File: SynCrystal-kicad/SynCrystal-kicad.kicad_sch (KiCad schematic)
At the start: 93 parts, among them CN1 PJ-342, J1 ICSP, J4 Pause Button, J5 to DIN-6 Male, J6 DIN-6 male, Q1 SS8050, Q2 SS8050, Q3 AO3400A, Q4 SS8050, SW1 Mode -, SW2 Mode +, SW3 Frame -, SW4 Frame +, SW6 Guide/Follow, U1 74HCT14, U10 MCP4725, U2 ATmega328P-A, U3 AP2210N-3.3TRG1, U4 ECS-TXO-3225MV-160-TR, U5 LMC6482, U7 G3VM-61VY3(TR)

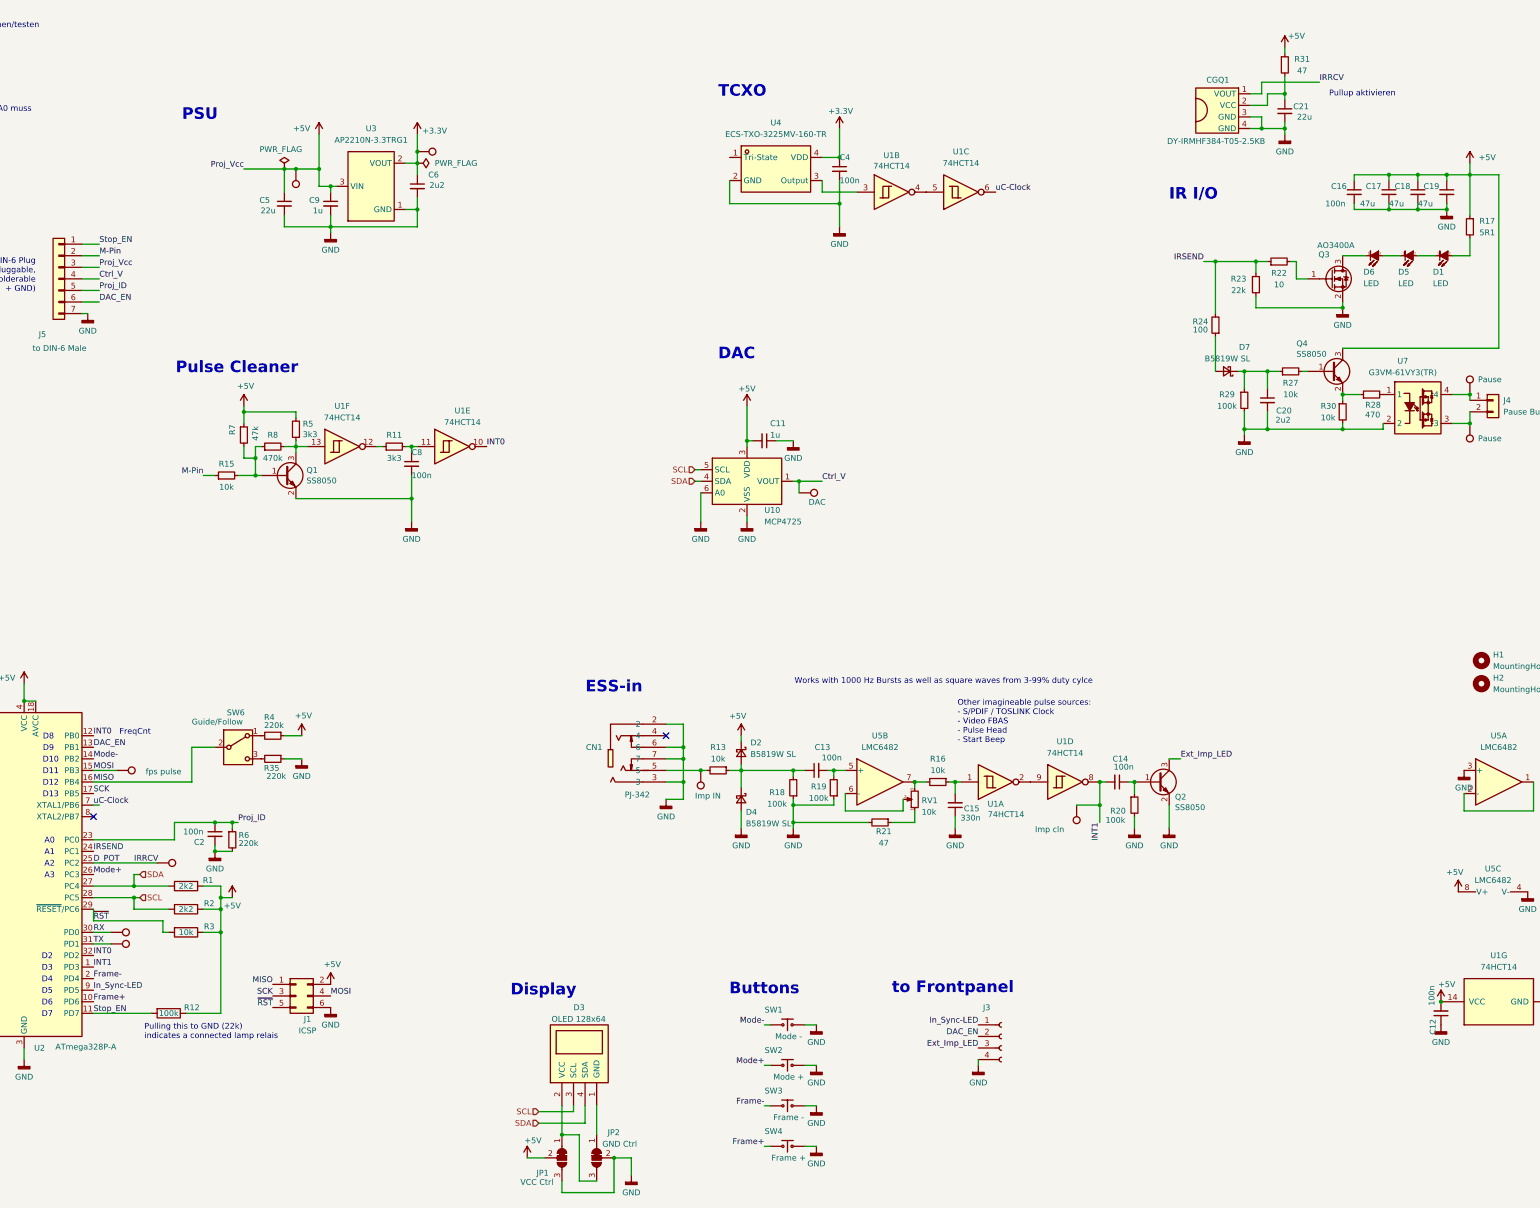
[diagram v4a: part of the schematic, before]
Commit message: ERC now happy!
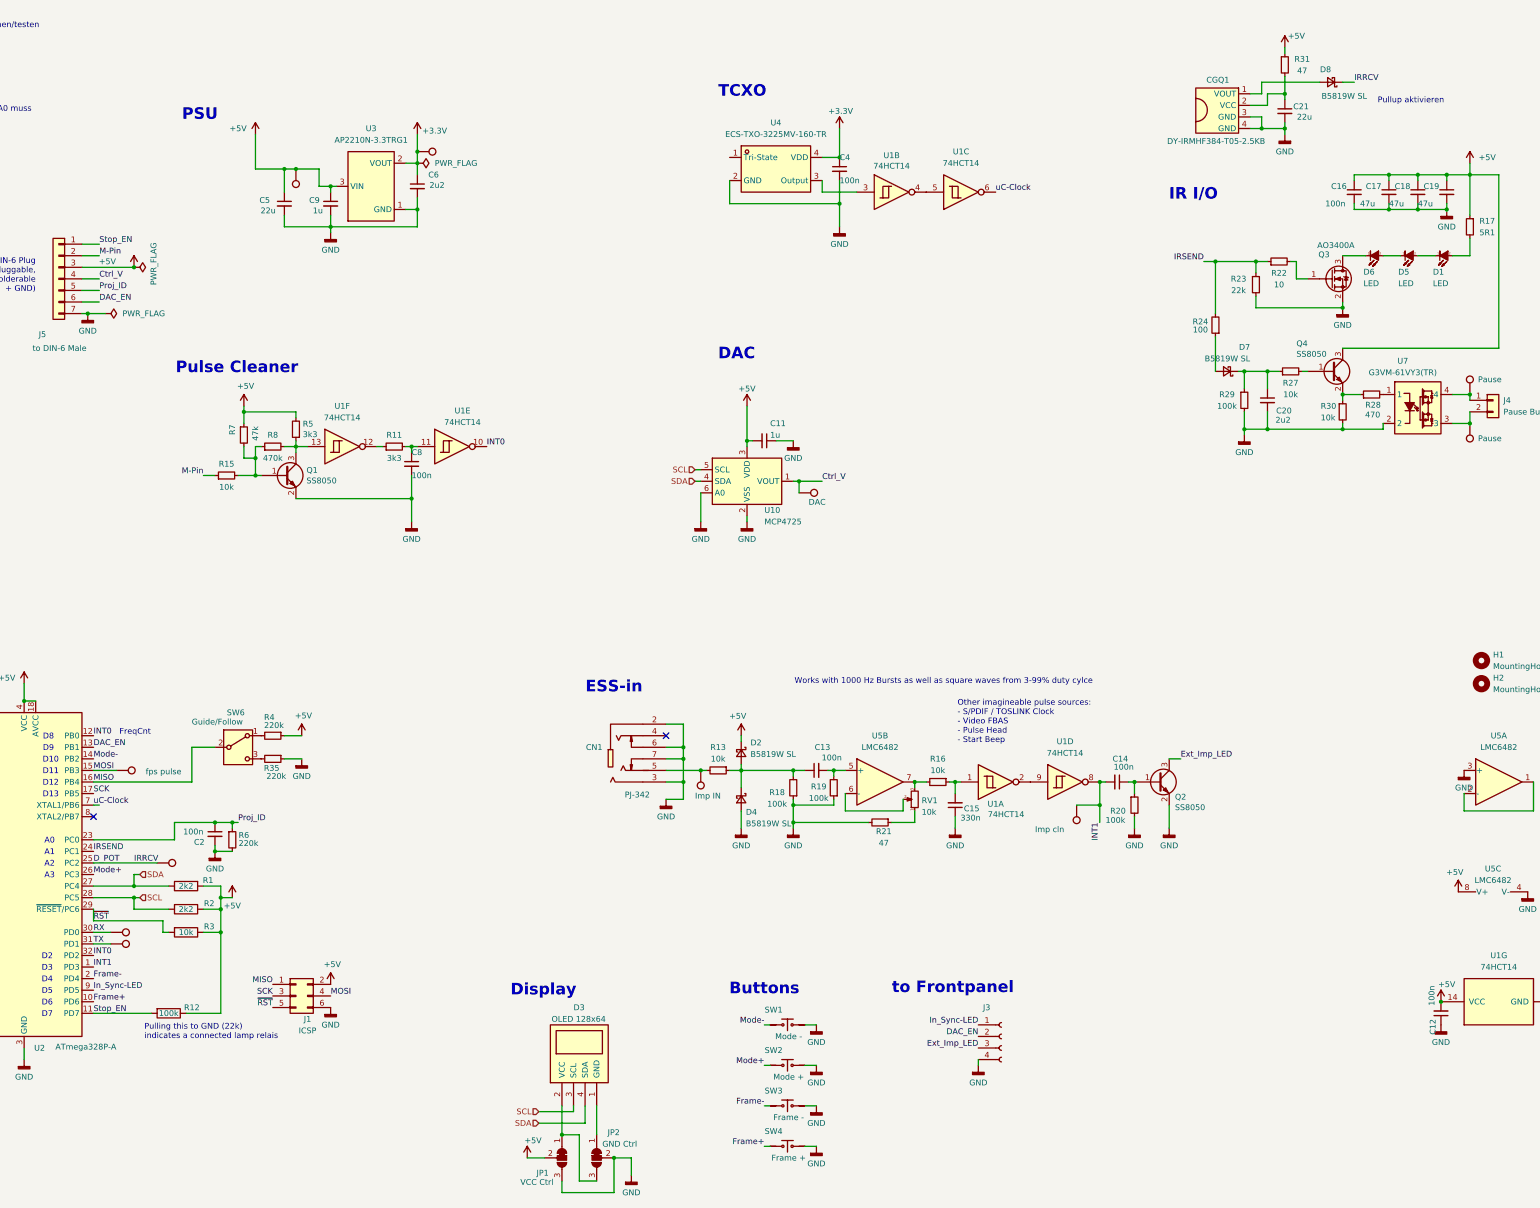
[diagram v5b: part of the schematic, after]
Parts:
- added D8: B5819W SL, Diode_SMD:D_SOD-123, symbol Device:D_Schottky_Small
- CGQ1: LCSC Part (none) -> C7280961
- CN1: LCSC Part (none) -> C668606
- D1, D5, D6: footprint easyEDA:LED-SMD_XYC-IRA4335A65-X4 -> easyeda2kicad:LED-SMD_XYC-IRA4335A65-X4
- SW1, SW2, SW3, SW4: footprint easyEDA:SW-SMD_4P-L6.0-W6.0-P4.50-LS9.0_TS-1002S-08026C -> easyEDA:KEY-SMD_4P-L6.0-W6.0-P4.50-LS8.6
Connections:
- net D_POT: now also D8.1 (K); no longer CGQ1.1 (VOUT)
- new net: CGQ1.1 (VOUT), D8.2 (A)

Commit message: Reannotated, PCB now messed up :)
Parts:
- D2: renamed from D6; footprint easyeda2kicad:LED-SMD_XYC-IRA4335A65-X4 -> easyEDA:LED-SMD_XYC-IRA4335A65-X4
- D3: renamed from D5; footprint easyeda2kicad:LED-SMD_XYC-IRA4335A65-X4 -> easyEDA:LED-SMD_XYC-IRA4335A65-X4
- D4: renamed from D1; footprint easyeda2kicad:LED-SMD_XYC-IRA4335A65-X4 -> easyEDA:LED-SMD_XYC-IRA4335A65-X4
- renumbered C21 to C1, C20 to C10, C8 to C12, C1 to C13, C13 to C14, C14 to C15, C15 to C16, C2 to C17, C12 to C18, C4 to C2, C6 to C3, C16 to C4, C17 to C5, C18 to C6, C19 to C7, C5 to C8, D8 to D1, D7 to D5, D2 to D6, D4 to D7, D3 to D8, J6 to J1, J5 to J2, J4 to J3, J1 to J4, J3 to J5, Q3 to Q1, Q4 to Q2, Q1 to Q3, Q2 to Q4, R31 to R1, R5 to R10, R7 to R11, R8 to R12, R11 to R13, R15 to R14, R4 to R15, R35 to R16, R13 to R17, R16 to R18, R18 to R19, R17 to R2, R19 to R20, R20 to R21, R21 to R22, R6 to R23, R1 to R24, R2 to R25, R3 to R26, R12 to R27, R22 to R3, R23 to R4, R24 to R5, R27 to R6, R28 to R7, R29 to R8, R30 to R9, SW6 to SW1, SW1 to SW2, SW2 to SW3, SW3 to SW4, SW4 to SW5, TP8 to TP1, TP11 to TP10, TP3 to TP11, TP4 to TP12, TP5 to TP13, TP7 to TP2, TP14 to TP3, TP13 to TP4, TP12 to TP5, TP1 to TP6, TP2 to TP7, TP6 to TP8, TP10 to TP9, U4 to U1, U3 to U2, U1 to U3, U7 to U4, U10 to U5, U5 to U6, U2 to U7

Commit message: 90% routed
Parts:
- removed TP3, TP4: Pause, TestPoint:TestPoint_Pad_D1.0mm, symbol Peacemans Teile:TestPoint_named
- added C19: 1u, Capacitor_SMD:C_0603_1608Metric, symbol Device:C_Small
- added H3, H4, H5, H6: MountingHole, MountingHole:MountingHole_3.2mm_M3_DIN965, symbol Mechanical:MountingHole
- H1, H2: footprint MountingHole:MountingHole_4.3mm_M4_ISO14580 -> MountingHole:MountingHole_3.2mm_M3_DIN965
- J4: footprint Connector_PinHeader_2.54mm:PinHeader_2x03_P2.54mm_Vertical_displaced+ -> Peacemans Teile:PinHeader_2x03_P2.54mm_Vertical_displaced
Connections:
- net +5V: now also C19.2
- net GND: now also C19.1
- net at J3.1 (Pin_1): now also U4.3; no longer U4.4
- net at J3.2 (Pin_2): now also U4.4; no longer U4.3
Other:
- note added: "To Do: - OpAmp-Rs auf Projektorboard neu berechnen/testen - Stop-Spannung messen - Monoflop auf Relaisplatine testen - Schottky an Lampe testen - INT1 wegsparen? (2 Schottkys) - Startpiepser statt ESS Impulen erkennen"
- note removed: "To Do: - OpAmp-Rs auf Projektorboard neu berechnen/testen - Stop-Spannung messen - Monoflop auf Relaisplatine testen - Schottky an Lampe testen - INT1 wegsparen? (2 Schottkys) - Startpiepser statt ESS Impulen erkennen Consider: - Projektor-Erkennung (für Imp-Ratio) über Spannungsteiler an DAC_EN, der dann an A0 muss"

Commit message: Looking good! Stil gotta run DRC
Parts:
- removed CN1: PJ-342, easyEDA:AUDIO-SMD_PJ-342, symbol easyEDA:PJ-342
- removed H2: MountingHole, MountingHole:MountingHole_3.2mm_M3_DIN965, symbol Mechanical:MountingHole
- added CN2: PJ-307N5, easyEDA:AUDIO-TH_PJ-307N5, symbol easyEDA:PJ-307N5
- H1: footprint MountingHole:MountingHole_3.2mm_M3_DIN965 -> Peacemans Teile:Kabelbinder 3mm
- SW1: footprint easyEDA:SW-TH_MSK12C02-HB-1 -> easyEDA:SW-TH_SS-12D11G4R; symbol Switch:SW_SPDT -> easyEDA:SS-12D11G4R; LCSC C431541 -> C843370; LCSC Part (none) -> C431541
- TP1, TP10, TP11, TP12, TP13, TP2, TP5, TP6, TP7, TP8, TP9: footprint TestPoint:TestPoint_Pad_D1.0mm -> TestPoint:TestPoint_THTPad_1.5x1.5mm_Drill0.7mm
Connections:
- net GND: now also CN2.1, CN2.2, CN2.5
- net at R17.2, TP9.1: now also CN2.4
- net at RV1.3, U6.7: now also R18.1; no longer R18.2
- net at C16.2, U3.1: now also R18.2; no longer R18.1
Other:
- moved on the sheet: R15, R16, R18, SW1
